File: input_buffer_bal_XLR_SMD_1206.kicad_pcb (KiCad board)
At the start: 2 copper layers, 62.5 x 52.5 mm, 31 parts, among them J1 CH1_XLR, J2 CH2_XLR, J3 POWER, J4 CH1_OUT, J5 CH2_OUT, U1 LM4562, U2 LM4562

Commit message: rev1.1 fixes major issues with the pcb layout
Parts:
- C1, C2, C3, C4, C5, C6, C7, C8: footprint Capacitor_SMD:C_1206_3216Metric -> Capacitor_SMD:C_1206_3216Metric_Pad1.42x1.75mm_HandSolder
- moved J1 1.27 mm to (103.8, 157.8)
- moved J2 1.27 mm to (138.8, 157.8)
- moved R10 1.25 mm to (140.5, 131.5)
- moved R5 1.25 mm to (105.0, 131.5)
- moved R6 1.25 mm to (137.5, 131.5)
- moved R7 1.25 mm to (102.0, 131.5)
- moved R8 1.25 mm to (108.0, 131.5)
- moved R9 1.25 mm to (134.5, 131.5)
- moved C5 0.50 mm to (97.0, 122.2)
- moved C6 0.50 mm to (113.0, 122.2)
- moved D1 0.50 mm to (97.0, 128.2)
- moved D2 0.50 mm to (113.0, 128.2)
- moved R1 0.50 mm to (97.0, 125.2)
- moved R2 0.50 mm to (113.0, 125.2)
- moved C4 0.35 mm to (136.5, 125.8)
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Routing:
- net GND: track 18.9 -> 0.00 mm, vias 270 -> 249
- net Net-(C6-Pad2): track 12.0 -> 14.0 mm
- net Net-(C5-Pad1): track 11.6 -> 13.5 mm
- net Net-(D2-Pad2): track 18.5 -> 20.0 mm
- net Net-(C8-Pad2): track 12.7 -> 13.9 mm
- net Net-(C7-Pad1): track 12.3 -> 13.5 mm
- net Net-(D4-Pad2): track 19.3 -> 18.1 mm
- net Net-(D3-Pad1): track 18.5 -> 19.2 mm
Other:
- board size 62.5 x 52.5 mm -> 62.5 x 49.8 mm
- board text added: "Bilous Sound"
- board text added: "May 2023"
- board text added: "Neutrik NC3FAAH2"
- board text added: "Rev 1.1"

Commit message: rev1.2 changed power connector
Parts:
- J3: footprint local_footprint_lib:TerminalBlock_ Amphenol_01_03_P3.50mm -> local_footprint_lib:TerminalBlock_ Amphenol_01_02_P3.50mm
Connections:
- J3 pad 1: -15V -> +15V
- J3 pad 2: GND -> -15V
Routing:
- net GND: vias 249 -> 251
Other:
- board text added: "June 2023"
- board text added: "Rev 1.2"
- board text removed: "May 2023"
- board text removed: "Rev 1.1"

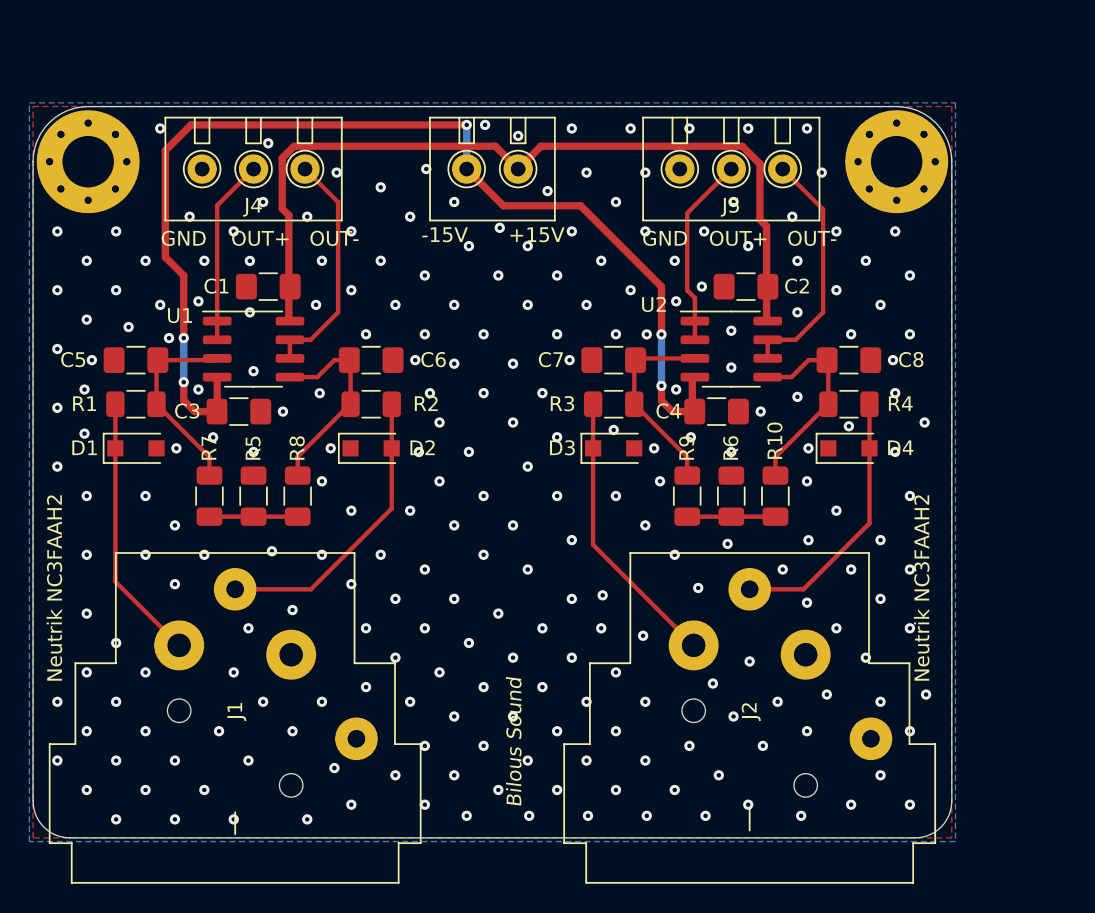
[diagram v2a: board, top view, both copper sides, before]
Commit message: revised with added option to change gain
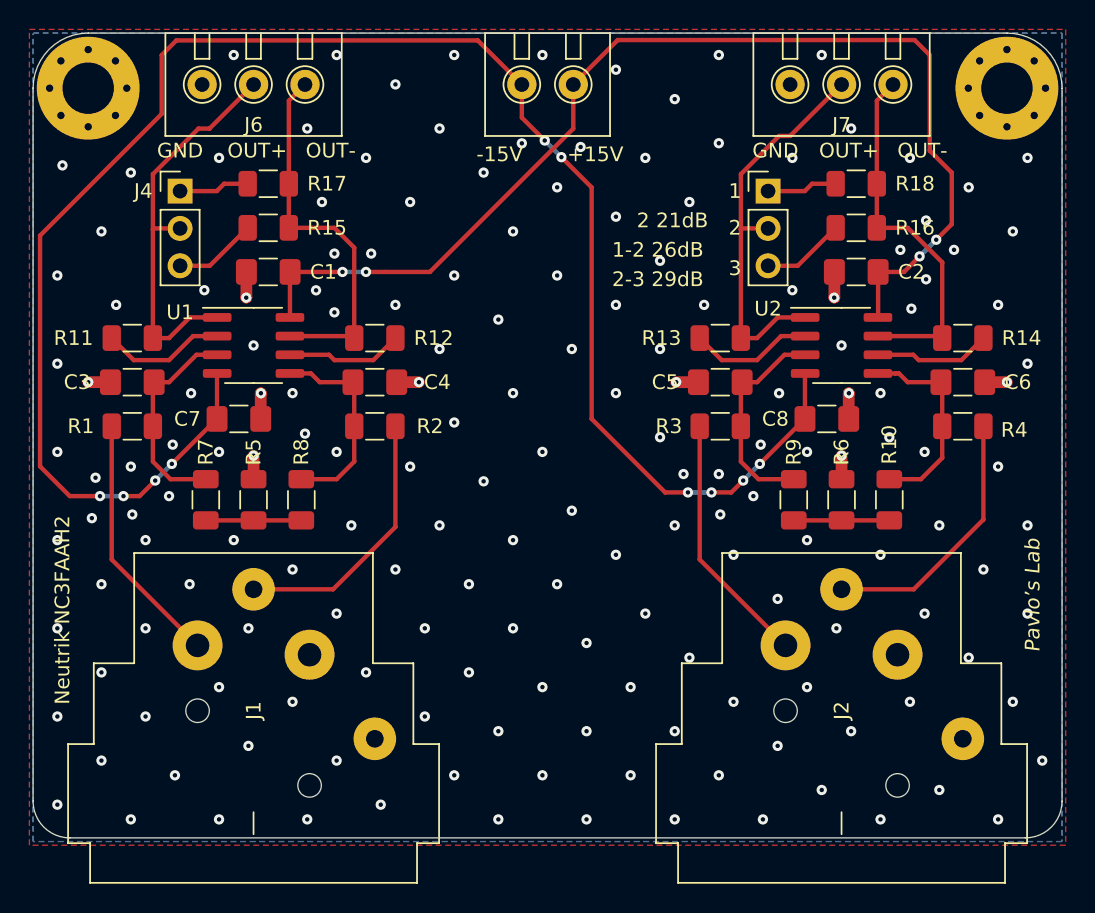
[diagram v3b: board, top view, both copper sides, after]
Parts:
- removed the C7 at (129.5, 122.2)
- removed the C8 at (145.5, 122.2)
- removed D1, D2, D3, D4: SMF6.0CA, Diode_SMD:D_SOD-123F
- added C5: 1n, Capacitor_SMD:C_1206_3216Metric_Pad1.42x1.75mm_HandSolder, F.Cu at (136.8, 123.8)
- added C6: 1n, Capacitor_SMD:C_1206_3216Metric_Pad1.42x1.75mm_HandSolder, F.Cu at (153.2, 123.8)
- added J6: CH1_OUT, local_footprint_lib:TerminalBlock_ Amphenol_01_03_P3.50mm, F.Cu at (105.0, 103.5)
- added J7: CH1_OUT, local_footprint_lib:TerminalBlock_ Amphenol_01_03_P3.50mm, F.Cu at (145.0, 103.5)
- added R11: 1K, Resistor_SMD:R_1206_3216Metric, F.Cu at (96.8, 120.8)
- added R12: 1K, Resistor_SMD:R_1206_3216Metric, F.Cu at (113.2, 120.8)
- added R13: 1K, Resistor_SMD:R_1206_3216Metric, F.Cu at (136.8, 120.8)
- added R14: 1K, Resistor_SMD:R_1206_3216Metric, F.Cu at (153.2, 120.8)
- added R15: 1K3, Resistor_SMD:R_1206_3216Metric, F.Cu at (106.0, 113.2)
- added R16: 1K3, Resistor_SMD:R_1206_3216Metric, F.Cu at (146.0, 113.2)
- added R17: 3k, Resistor_SMD:R_1206_3216Metric, F.Cu at (106.0, 110.2)
- added R18: 3k, Resistor_SMD:R_1206_3216Metric, F.Cu at (146.0, 110.2)
- C3: renamed from C5; value 220p -> 1n
- C4: renamed from C6; value 220p -> 1n
- J4: value CH1_OUT -> Gain; footprint local_footprint_lib:TerminalBlock_ Amphenol_01_03_P3.50mm -> Connector_PinHeader_2.54mm:PinHeader_1x03_P2.54mm_Vertical
- J5: value CH2_OUT -> Gain; footprint local_footprint_lib:TerminalBlock_ Amphenol_01_03_P3.50mm -> Connector_PinHeader_2.54mm:PinHeader_1x03_P2.54mm_Vertical
- moved H2 9.01 mm to (156.2, 103.8)
- moved R4 7.89 mm to (153.2, 126.8)
- moved R10 7.75 mm to (148.2, 131.8)
- moved C2 7.57 mm to (146.0, 116.2)
- moved C8 7.52 mm to (144.0, 126.2)
- moved R6 7.50 mm to (145.0, 131.8)
- moved U2 7.50 mm to (145.0, 121.2)
- moved R3 7.40 mm to (136.8, 126.8)
- moved R9 7.25 mm to (141.8, 131.8)
- moved J3 6.86 mm to (125.0, 103.5)
- moved J2 6.25 mm to (145.0, 157.8)
- moved J4 5.22 mm to (100.0, 110.8), turned to 0 degrees
- moved H1 5.00 mm to (93.8, 103.8)
- moved J5 2.92 mm to (140.0, 110.8), turned to 0 degrees
- moved C3 1.52 mm to (96.8, 123.8)
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- renumbered C3 to C7, C4 to C8
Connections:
- J4 pad 3: GND -> Net-(J4-Pad3)
- J5 pad 3: GND -> Net-(J5-Pad3)
- U1 pad 2: Net-(J4-Pad2) -> Net-(R11-Pad2)
- U1 pad 6: Net-(J4-Pad1) -> Net-(R12-Pad2)
- U1 pad 7: Net-(J4-Pad1) -> Net-(J6-Pad1)
- U2 pad 2: Net-(J5-Pad2) -> Net-(R13-Pad2)
- U2 pad 6: Net-(J5-Pad1) -> Net-(R14-Pad2)
- U2 pad 7: Net-(J5-Pad1) -> Net-(J7-Pad1)
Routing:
- net -15V: track 76.4 -> 122.2 mm, vias 5 -> 10
- net Net-(J6-Pad1): track 0.00 -> 25.8 mm
- net Net-(J7-Pad1): track 0.00 -> 25.2 mm
- net +15V: track 56.8 -> 76.9 mm, vias 0 -> 4
- net GND: track 0.00 -> 16.3 mm, vias 251 -> 177
- net Net-(J4-Pad2): track 12.6 -> 27.4 mm
- net Net-(J5-Pad2): track 13.1 -> 27.4 mm
- net Net-(J5-Pad1): track 16.7 -> 4.81 mm
- net Net-(J4-Pad1): track 16.0 -> 4.81 mm
- net Net-(R13-Pad2): track 0.00 -> 8.47 mm
- net Net-(R11-Pad2): track 0.00 -> 8.47 mm
- net Net-(R12-Pad2): track 0.00 -> 7.95 mm
- net Net-(R14-Pad2): track 0.00 -> 7.95 mm
- net Net-(J5-Pad3): track 0.00 -> 5.67 mm
- net Net-(J4-Pad3): track 0.00 -> 5.67 mm
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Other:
- board size 62.5 x 49.8 mm -> 70 x 54.8 mm
- board text added: "1"
- board text added: "1-2 26dB"
- board text added: "2"
- board text added: "2 21dB"
- board text added: "2-3 29dB"
- board text added: "3"
- board text added: "January 2024"
- board text added: "Pavlo’s Lab"
- board text added: "Rev 2.0"
- board text removed: "Bilous Sound"
- board text removed: "June 2023"
- board text removed: "Rev 1.2"
